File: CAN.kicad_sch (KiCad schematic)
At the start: 34 parts, among them U7 MCP2515-xST, U8 SN65HVD230, Y1 16MHz

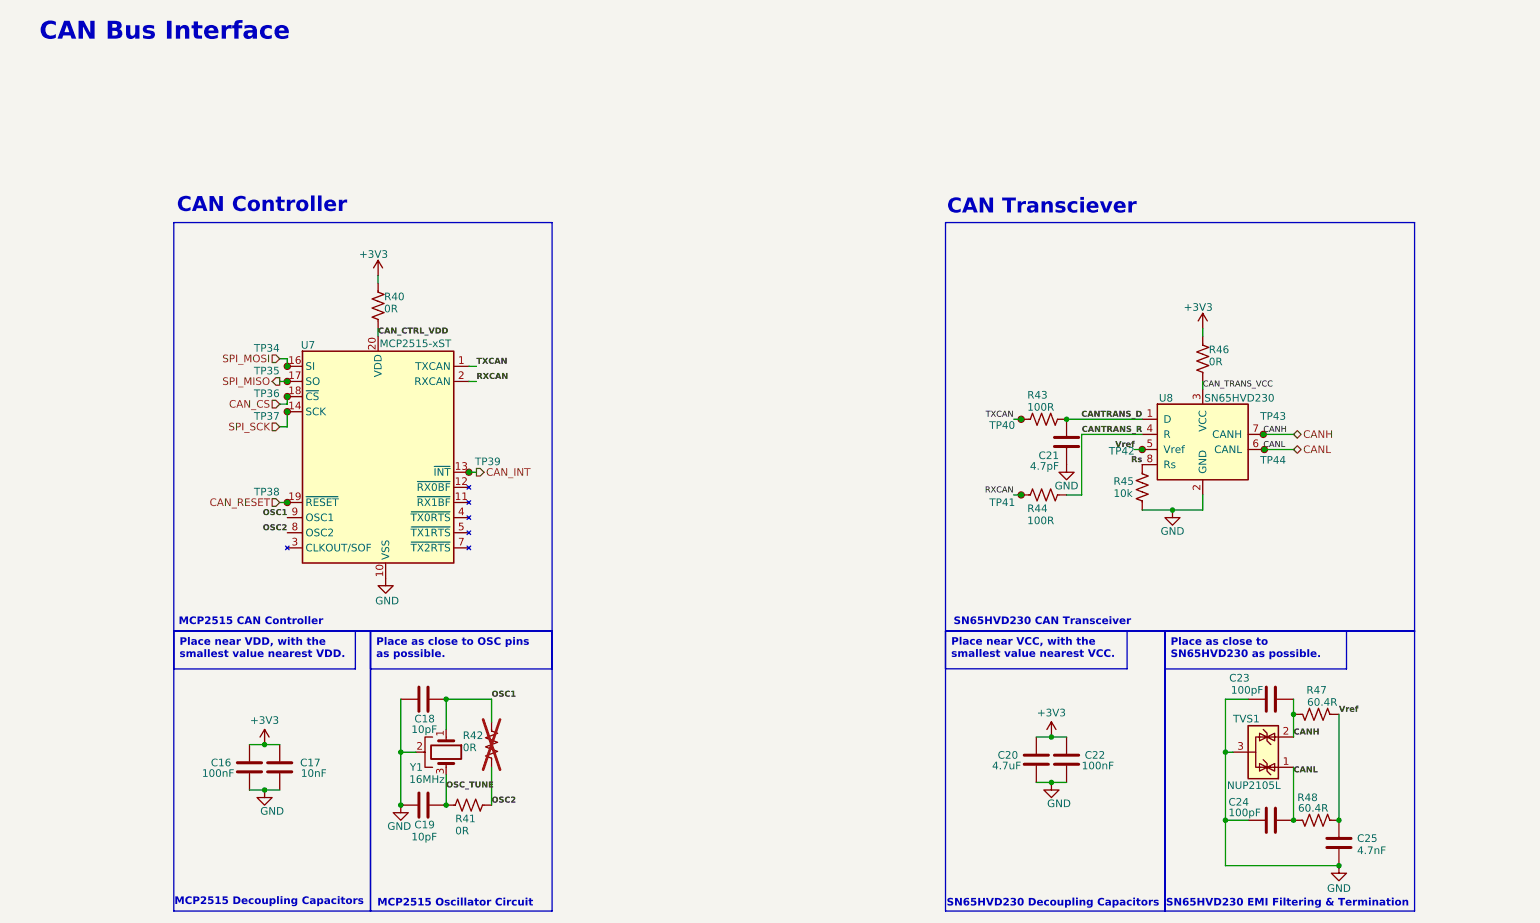
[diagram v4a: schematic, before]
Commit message: Started work on PCB layout
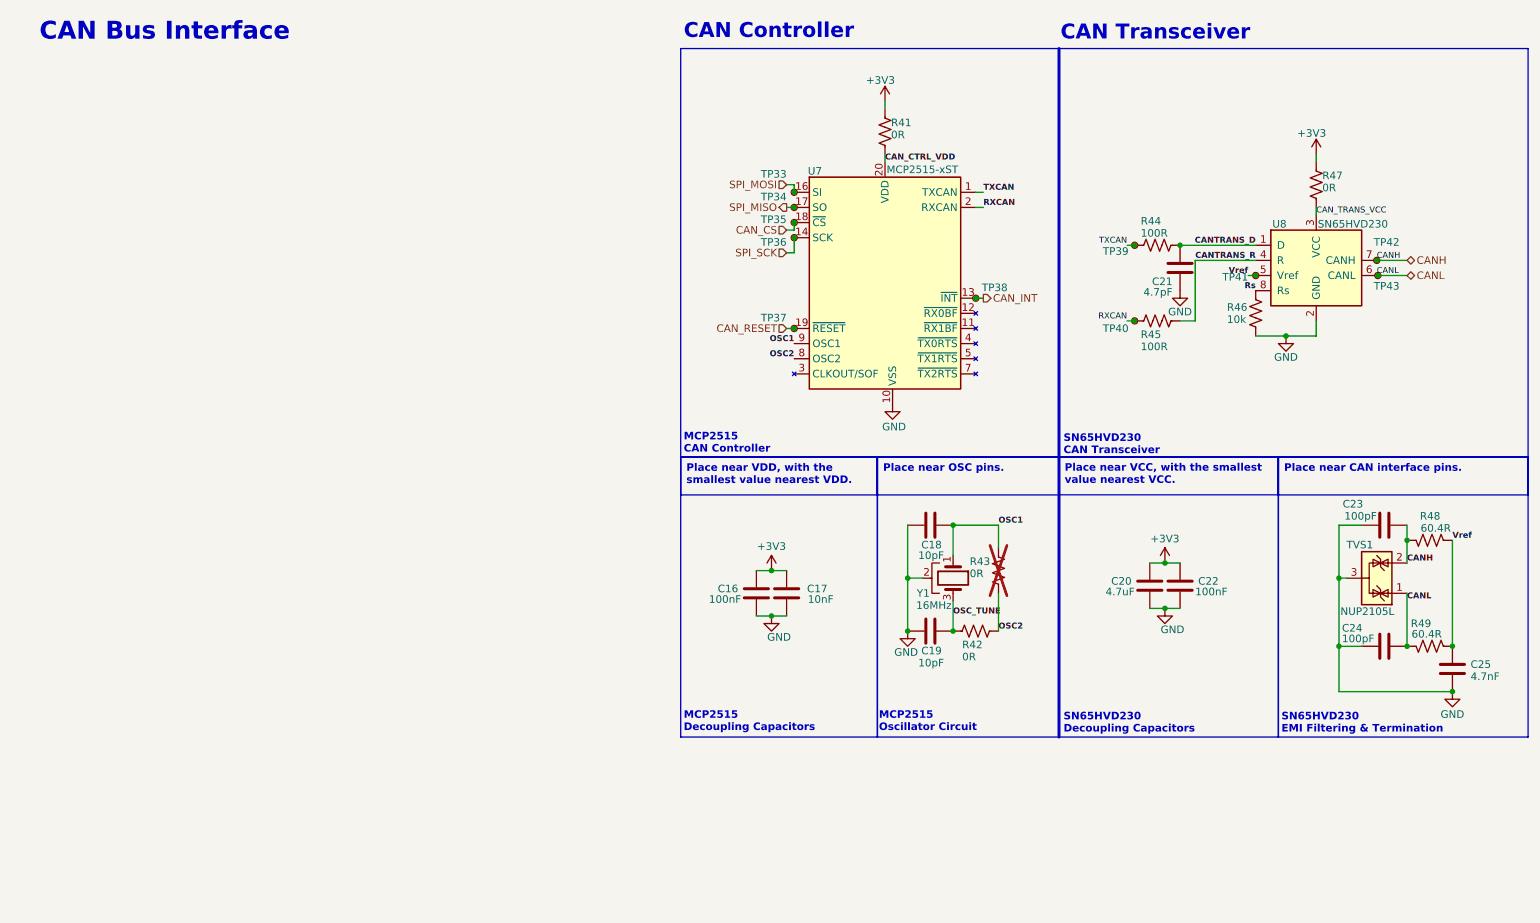
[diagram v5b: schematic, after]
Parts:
- TP37: renamed from TP38; footprint (none) -> TestPoint:TestPoint_Pad_D1.0mm
- TP38: renamed from TP39; footprint (none) -> TestPoint:TestPoint_Pad_D1.0mm
- renumbered R40 to R41, R41 to R42, R42 to R43, R43 to R44, R44 to R45, R45 to R46, R46 to R47, R47 to R48, R48 to R49, TP34 to TP33, TP35 to TP34, TP36 to TP35, TP37 to TP36, TP40 to TP39, TP41 to TP40, TP42 to TP41, TP43 to TP42, TP44 to TP43
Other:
- note added: "CAN Transceiver"
- note removed: "CAN Transciever"
- moved on the sheet: C16, C17, C18, C19, C20, C21, C22, C23, C24, C25, R41, R42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

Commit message: Initial commit
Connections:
- net +3V3: no longer C16.2, C17.2, C20.2, C22.2
- net CAN_CTRL_VDD: now also C16.2, C17.2
- net CAN_TRANS_VCC: now also C20.2, C22.2
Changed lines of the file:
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@@
 	)
 	(junction
+		(at 135.89 106.68)
+		(diameter 0)
+		(color 0 0 0 0)
+	)
+	(junction
 		(at 139.7 66.04)
 		(diameter 0)
@@
 	)
 	(junction
+		(at 201.93 105.41)
+		(diameter 0)
+		(color 0 0 0 0)
+	)
+	(junction
 		(at 196.85 64.77)
 		(diameter 0)
@@
 	)
 	(junction
-		(at 201.93 105.41)
-		(diameter 0)
-		(color 0 0 0 0)
-	)
-	(junction
 		(at 139.7 43.18)
 		(diameter 0)
@@
 	)
 	(junction
-		(at 135.89 106.68)
-		(diameter 0)
-		(color 0 0 0 0)
-	)
-	(junction
 		(at 237.49 54.61)
 		(diameter 0)
@@
 	(wire
 		(pts
+			(xy 201.93 102.87) (xy 201.93 105.41)
+		)
+		(stroke
+			(width 0)
+			(type default)
+		)
+	)
+	(wire
+		(pts
 			(xy 215.9 57.15) (xy 217.17 57.15)
 		)
@@
 	(wire
 		(pts
-			(xy 133.35 106.68) (xy 135.89 106.68)
+			(xy 171.45 45.72) (xy 170.18 45.72)
 		)
 		(stroke
@@
 	(wire
 		(pts
-			(xy 171.45 45.72) (xy 170.18 45.72)
+			(xy 138.43 114.3) (xy 135.89 114.3)
 		)
 		(stroke
@@
 	(wire
 		(pts
-			(xy 138.43 114.3) (xy 135.89 114.3)
+			(xy 173.99 110.49) (xy 173.99 116.84)
 		)
 		(stroke
@@
 	(wire
 		(pts
-			(xy 173.99 110.49) (xy 173.99 116.84)
+			(xy 242.57 54.61) (xy 237.49 54.61)
 		)
 		(stroke
@@
 	(wire
 		(pts
-			(xy 242.57 54.61) (xy 237.49 54.61)
+			(xy 138.43 41.91) (xy 139.7 41.91)
 		)
 		(stroke
@@
 	(wire
 		(pts
-			(xy 138.43 41.91) (xy 139.7 41.91)
+			(xy 158.75 99.06) (xy 158.75 107.95)
 		)
 		(stroke
@@
 	(wire
 		(pts
-			(xy 158.75 99.06) (xy 158.75 107.95)
+			(xy 135.89 105.41) (xy 135.89 106.68)
 		)
 		(stroke
@@
 	(wire
 		(pts
-			(xy 201.93 105.41) (xy 204.47 105.41)
+			(xy 227.33 36.83) (xy 227.33 38.1)
 		)
 		(stroke
@@
 	(wire
 		(pts
-			(xy 227.33 36.83) (xy 227.33 38.1)
+			(xy 138.43 45.72) (xy 139.7 45.72)
 		)
 		(stroke
@@
 	(wire
 		(pts
-			(xy 138.43 45.72) (xy 139.7 45.72)
+			(xy 207.01 64.77) (xy 207.01 54.61)
 		)
 		(stroke
@@
 	(wire
 		(pts
-			(xy 207.01 64.77) (xy 207.01 54.61)
+			(xy 231.14 107.95) (xy 231.14 99.06)
 		)
 		(stroke
@@
 	(wire
 		(pts
-			(xy 231.14 107.95) (xy 231.14 99.06)
+			(xy 133.35 106.68) (xy 135.89 106.68)
 		)
 		(stroke
@@
 	(wire
 		(pts
-			(xy 135.89 106.68) (xy 138.43 106.68)
+			(xy 173.99 99.06) (xy 166.37 99.06)
 		)
 		(stroke
@@
 	(wire
 		(pts
-			(xy 173.99 99.06) (xy 166.37 99.06)
+			(xy 139.7 53.34) (xy 139.7 50.8)
 		)
 		(stroke
@@
 	(wire
 		(pts
-			(xy 139.7 53.34) (xy 139.7 50.8)
+			(xy 234.95 119.38) (xy 231.14 119.38)
 		)
 		(stroke
@@
 	(wire
 		(pts
-			(xy 234.95 119.38) (xy 231.14 119.38)
+			(xy 201.93 105.41) (xy 204.47 105.41)
 		)
 		(stroke
@@
 	(wire
 		(pts
+			(xy 135.89 106.68) (xy 138.43 106.68)
+		)
+		(stroke
+			(width 0)
+			(type default)
+		)
+	)
+	(wire
+		(pts
 			(xy 217.17 67.31) (xy 222.25 67.31)
 		)
@@
 		)
 	)
+	(label "CAN_CTRL_VDD"
+		(at 135.89 105.41 0)
+		(effects
+			(font
+				(size 1 1)
+				(thickness 0.2)
+				(bold yes)
+			)
+			(justify left bottom)
+		)
+	)
 	(label "CANL"
 		(at 237.49 57.15 0)
@@
 		)
 	)
+	(label "CAN_TRANS_VCC"
+		(at 201.93 102.87 0)
+		(effects
+			(font
+				(size 1 1)
+			)
+			(justify left bottom)
+		)
+	)
 	(label "RXCAN"
 		(at 195.58 64.77 180)
@@
 				)
 			)
-		)
-	)
-	(symbol
-		(lib_id "power:+3V3")
-		(at 201.93 105.41 0)
-		(unit 1)
-		(body_style 1)
-		(exclude_from_sim no)
-		(in_bom yes)
-		(on_board yes)
-		(in_pos_files yes)
-		(dnp no)
-		(property "Reference" "#PWR049"
-			(at 201.93 109.22 0)
-			(hide yes)
-			(show_name no)
-			(do_not_autoplace no)
-			(effects
-				(font
-					(size 1.27 1.27)
-				)
-			)
-		)
-		(property "Value" "+3V3"
-			(at 201.93 101.346 0)
-			(show_name no)
-			(do_not_autoplace no)
-			(effects
-				(font
-					(size 1.27 1.27)
-				)
-			)
-		)
-		(property "Footprint" ""
-			(at 201.93 105.41 0)
-			(hide yes)
-			(show_name no)
-			(do_not_autoplace no)
-			(effects
-				(font
-					(size 1.27 1.27)
-				)
-			)
-		)
-		(property "Datasheet" ""
-			(at 201.93 105.41 0)
-			(hide yes)
-			(show_name no)
-			(do_not_autoplace no)
-			(effects
-				(font
-					(size 1.27 1.27)
-				)
-			)
-		)
-		(property "Description" "Power symbol creates a global label with name \"+3V3\""
-			(at 201.93 105.41 0)
-			(hide yes)
-			(show_name no)
-			(do_not_autoplace no)
-			(effects
-				(font
-					(size 1.27 1.27)
-				)
-			)
-		)
-		(pin "1"
-		)
-		(instances
-			(project "power_module"
-				(path "/33e2b92e-f705-4be7-96f4-57092b8ec1ea/2c777b8c-fce7-4c8f-b22a-e5c1ebb4dbeb"
-					(reference "#PWR049")
-					(unit 1)
-				)
-			)
-		)
-	)
-	(symbol
-		(lib_id "power:+3V3")
-		(at 135.89 106.68 0)
-		(unit 1)
-		(body_style 1)
-		(exclude_from_sim no)
-		(in_bom yes)
-		(on_board yes)
-		(in_pos_files yes)
-		(dnp no)
-		(property "Reference" "#PWR044"
-			(at 135.89 110.49 0)
-			(hide yes)
-			(show_name no)
-			(do_not_autoplace no)
-			(effects
-				(font
-					(size 1.27 1.27)
-				)
-			)
-		)
-		(property "Value" "+3V3"
-			(at 135.89 102.616 0)
-			(show_name no)
-			(do_not_autoplace no)
-			(effects
-				(font
-					(size 1.27 1.27)
-				)
-			)
-		)
-		(property "Footprint" ""
-			(at 135.89 106.68 0)
-			(hide yes)
-			(show_name no)
-			(do_not_autoplace no)
-			(effects
-				(font
-					(size 1.27 1.27)
-				)
-			)
-		)
-		(property "Datasheet" ""
-			(at 135.89 106.68 0)
-			(hide yes)
-			(show_name no)
-			(do_not_autoplace no)
-			(effects
-				(font
-					(size 1.27 1.27)
-				)
-			)
-		)
-		(property "Description" "Power symbol creates a global label with name \"+3V3\""
-			(at 135.89 106.68 0)
-			(hide yes)
-			(show_name no)
-			(do_not_autoplace no)
-			(effects
-				(font
-					(size 1.27 1.27)
-				)
-			)
-		)
-		(pin "1"
-		)
-		(instances
-			(project "power_module"
-				(path "/33e2b92e-f705-4be7-96f4-57092b8ec1ea/2c777b8c-fce7-4c8f-b22a-e5c1ebb4dbeb"
-					(reference "#PWR044")
-					(unit 1)
-				)
-			)
